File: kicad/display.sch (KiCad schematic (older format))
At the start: 19 parts, among them Q1 2N3906, Q2 2N3906, Q3 2N3906, Q4 2N3906, Q5 2N3906

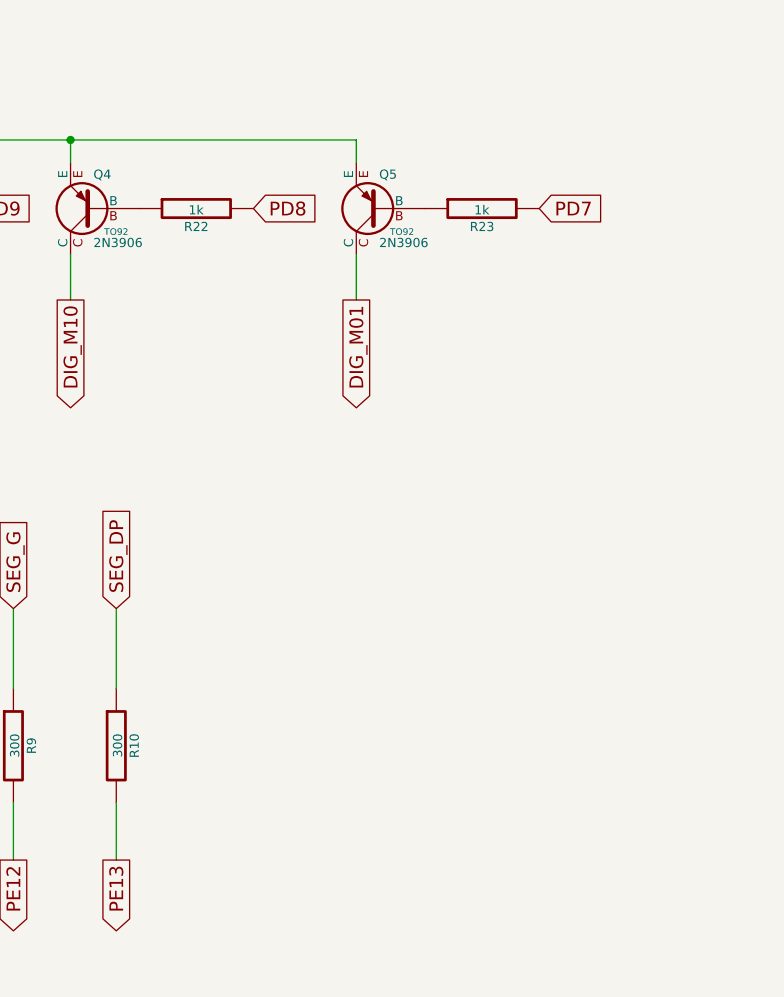
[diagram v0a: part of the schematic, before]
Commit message: Final routing
Removed some intermediary routing steps, too
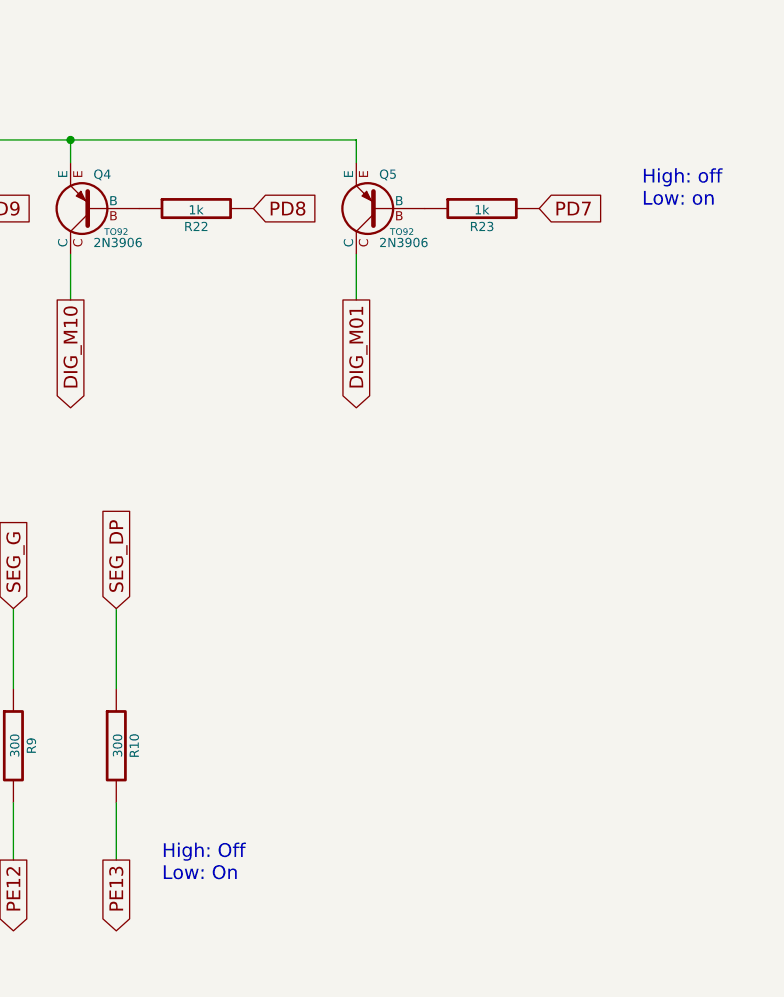
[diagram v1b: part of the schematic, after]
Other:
- note added: "High: Off\nLow: On"
- note added: "High: off\nLow: on"
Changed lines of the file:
@@
 Sheet 4 5
 Title ""
-Date "18 jun 2015"
+Date "19 jun 2015"
 Rev ""
 Comp ""
@@
 Text GLabel 5000 1150 0    60   Input ~ 0
 3V_205
+Text Notes 9650 3500 0    60   ~ 0
+High: off\nLow: on
+Text Notes 7550 6450 0    60   ~ 0
+High: Off\nLow: On
 $EndSCHEMATC

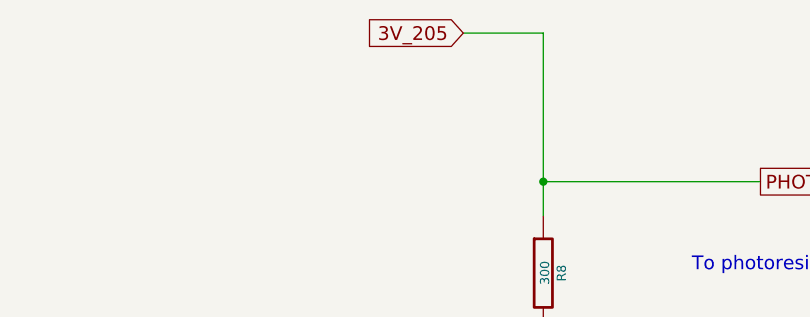
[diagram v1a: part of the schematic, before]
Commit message: *Fix* Missing IO pins
Added PA4 to the schematic IO page and fixed PD8, PD10
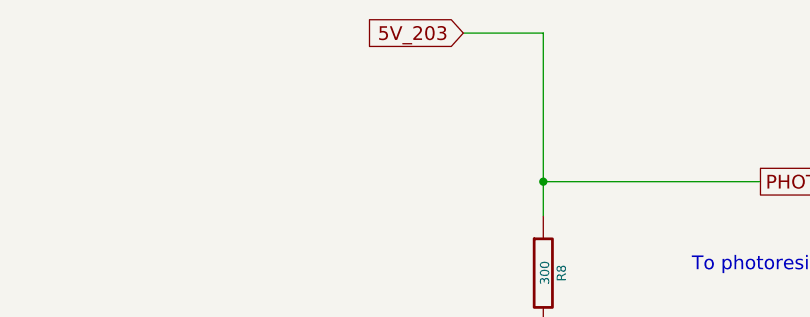
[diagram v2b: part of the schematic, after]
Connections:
- net 3V_205 renamed 5V_203
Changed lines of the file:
@@
 Sheet 4 5
 Title ""
-Date "19 jun 2015"
+Date "30 jun 2015"
 Rev ""
 Comp ""
@@
 To STM control pins
 Text GLabel 5000 1150 0    60   Input ~ 0
-3V_205
+5V_203
 Text Notes 9650 3500 0    60   ~ 0
 High: off\nLow: on
